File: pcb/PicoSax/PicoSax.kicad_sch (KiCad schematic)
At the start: 73 parts, among them J3 Conn_01x02, SW8va1 Omron_B3K_L13L, SW8vb1 Omron_B3K_L13L, U1 Perfboard

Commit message: Clean and Parts BOM
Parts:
- R16: footprint Resistor_THT:R_Axial_DIN0204_L3.6mm_D1.6mm_P7.62mm_Horizontal -> Resistor_SMD:R_1210_3225Metric_Pad1.30x2.65mm_HandSolder
- R17: footprint Resistor_THT:R_Axial_DIN0204_L3.6mm_D1.6mm_P7.62mm_Horizontal -> Resistor_SMD:R_0805_2012Metric_Pad1.20x1.40mm_HandSolder
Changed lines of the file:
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@@
 			)
 		)
-		(property "Footprint" "Resistor_THT:R_Axial_DIN0204_L3.6mm_D1.6mm_P7.62mm_Horizontal"
+		(property "Footprint" "Resistor_SMD:R_1210_3225Metric_Pad1.30x2.65mm_HandSolder"
 			(at 135.382 73.66 90)
 			(effects
@@
 			)
 		)
-		(property "Footprint" "Resistor_THT:R_Axial_DIN0204_L3.6mm_D1.6mm_P7.62mm_Horizontal"
+		(property "Footprint" "Resistor_SMD:R_0805_2012Metric_Pad1.20x1.40mm_HandSolder"
 			(at 135.382 83.82 90)
 			(effects

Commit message: v0.2
Updated LED footprint to have correct pin numbering.  Redid layout and traces. Added helpful silkscreen for pi pico.  Added some datasheets.
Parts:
- D10: renamed from L9; footprint MyLibrary:19-C47&slash_RSGHBHC-5V01&slash_2T_EVE-M -> PicoSax:19-C47_RSGHBHC-5V01-2T
- D11: renamed from L10; footprint MyLibrary:19-C47&slash_RSGHBHC-5V01&slash_2T_EVE-M -> PicoSax:19-C47_RSGHBHC-5V01-2T
- D12: renamed from L11; footprint MyLibrary:19-C47&slash_RSGHBHC-5V01&slash_2T_EVE-M -> PicoSax:19-C47_RSGHBHC-5V01-2T
- D13: renamed from L12; footprint MyLibrary:19-C47&slash_RSGHBHC-5V01&slash_2T_EVE-M -> PicoSax:19-C47_RSGHBHC-5V01-2T
- D14: renamed from L13; footprint MyLibrary:19-C47&slash_RSGHBHC-5V01&slash_2T_EVE-M -> PicoSax:19-C47_RSGHBHC-5V01-2T
- D2: renamed from L1; footprint MyLibrary:19-C47&slash_RSGHBHC-5V01&slash_2T_EVE-M -> PicoSax:19-C47_RSGHBHC-5V01-2T
- D3: renamed from L2; footprint MyLibrary:19-C47&slash_RSGHBHC-5V01&slash_2T_EVE-M -> PicoSax:19-C47_RSGHBHC-5V01-2T
- D4: renamed from L3; footprint MyLibrary:19-C47&slash_RSGHBHC-5V01&slash_2T_EVE-M -> PicoSax:19-C47_RSGHBHC-5V01-2T
- D5: renamed from L4; footprint MyLibrary:19-C47&slash_RSGHBHC-5V01&slash_2T_EVE-M -> PicoSax:19-C47_RSGHBHC-5V01-2T
- D6: renamed from L5; footprint MyLibrary:19-C47&slash_RSGHBHC-5V01&slash_2T_EVE-M -> PicoSax:19-C47_RSGHBHC-5V01-2T
- D7: renamed from L6; footprint MyLibrary:19-C47&slash_RSGHBHC-5V01&slash_2T_EVE-M -> PicoSax:19-C47_RSGHBHC-5V01-2T
- D8: renamed from L7; footprint MyLibrary:19-C47&slash_RSGHBHC-5V01&slash_2T_EVE-M -> PicoSax:19-C47_RSGHBHC-5V01-2T
- D9: renamed from L8; footprint MyLibrary:19-C47&slash_RSGHBHC-5V01&slash_2T_EVE-M -> PicoSax:19-C47_RSGHBHC-5V01-2T
- J2: footprint MyLibrary:MIDI_DIN5 -> PicoSax:MIDI_DIN5
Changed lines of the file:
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@@
 		(dnp no)
 		(fields_autoplaced yes)
-		(property "Reference" "L4"
+		(property "Reference" "D5"
 			(at 283.21 143.51 0)
 			(effects
@@
 			)
 		)
-		(property "Footprint" "MyLibrary:19-C47&slash_RSGHBHC-5V01&slash_2T_EVE-M"
+		(property "Footprint" "PicoSax:19-C47_RSGHBHC-5V01-2T"
 			(at 265.684 141.732 0)
 			(effects
@@
 			(project "PicoSax"
 				(path "/ef0a1a94-772b-4785-b748-662adf24a5cd"
-					(reference "L4")
+					(reference "D5")
 					(unit 1)
 				)
@@
 		(dnp no)
 		(fields_autoplaced yes)
-		(property "Reference" "L13"
+		(property "Reference" "D14"
 			(at 353.06 184.15 0)
 			(effects
@@
 			)
 		)
-		(property "Footprint" "MyLibrary:19-C47&slash_RSGHBHC-5V01&slash_2T_EVE-M"
+		(property "Footprint" "PicoSax:19-C47_RSGHBHC-5V01-2T"
 			(at 335.534 182.372 0)
 			(effects
@@
 			(project "PicoSax"
 				(path "/ef0a1a94-772b-4785-b748-662adf24a5cd"
-					(reference "L13")
+					(reference "D14")
 					(unit 1)
 				)
@@
 		(dnp no)
 		(fields_autoplaced yes)
-		(property "Reference" "L9"
+		(property "Reference" "D10"
 			(at 353.06 102.87 0)
 			(effects
@@
 			)
 		)
-		(property "Footprint" "MyLibrary:19-C47&slash_RSGHBHC-5V01&slash_2T_EVE-M"
+		(property "Footprint" "PicoSax:19-C47_RSGHBHC-5V01-2T"
 			(at 335.534 101.092 0)
 			(effects
@@
 			(project "PicoSax"
 				(path "/ef0a1a94-772b-4785-b748-662adf24a5cd"
-					(reference "L9")
+					(reference "D10")
 					(unit 1)
 				)
@@
 			)
 		)
-		(property "Footprint" "MyLibrary:MIDI_DIN5"
+		(property "Footprint" "PicoSax:MIDI_DIN5"
 			(at 152.4 67.31 0)
 			(effects
@@
 		(dnp no)
 		(fields_autoplaced yes)
-		(property "Reference" "L6"
+		(property "Reference" "D7"
 			(at 283.21 184.15 0)
 			(effects
@@
 			)
 		)
-		(property "Footprint" "MyLibrary:19-C47&slash_RSGHBHC-5V01&slash_2T_EVE-M"
+		(property "Footprint" "PicoSax:19-C47_RSGHBHC-5V01-2T"
 			(at 265.684 182.372 0)
 			(effects
@@
 			(project ""
 				(path "/ef0a1a94-772b-4785-b748-662adf24a5cd"
-					(reference "L6")
+					(reference "D7")
 					(unit 1)
 				)
@@
 		(dnp no)
 		(fields_autoplaced yes)
-		(property "Reference" "L5"
+		(property "Reference" "D6"
 			(at 283.21 163.83 0)
 			(effects
@@
 			)
 		)
-		(property "Footprint" "MyLibrary:19-C47&slash_RSGHBHC-5V01&slash_2T_EVE-M"
+		(property "Footprint" "PicoSax:19-C47_RSGHBHC-5V01-2T"
 			(at 265.684 162.052 0)
 			(effects
@@
 			(project "PicoSax"
 				(path "/ef0a1a94-772b-4785-b748-662adf24a5cd"
-					(reference "L5")
+					(reference "D6")
 					(unit 1)
 				)
@@
 		(dnp no)
 		(fields_autoplaced yes)
-		(property "Reference" "L10"
+		(property "Reference" "D11"
 			(at 353.06 123.19 0)
 			(effects
@@
 			)
 		)
-		(property "Footprint" "MyLibrary:19-C47&slash_RSGHBHC-5V01&slash_2T_EVE-M"
+		(property "Footprint" "PicoSax:19-C47_RSGHBHC-5V01-2T"
 			(at 335.534 121.412 0)
 			(effects
@@
 			(project "PicoSax"
 				(path "/ef0a1a94-772b-4785-b748-662adf24a5cd"
-					(reference "L10")
+					(reference "D11")
 					(unit 1)
 				)
@@
 	)
 	(symbol
-		(lib_name "MP3V5004GP_1")
 		(lib_id "PicoSax:MP3V5004GP_1")
 		(at 212.09 187.96 0)
@@
 		(dnp no)
 		(fields_autoplaced yes)
-		(property "Reference" "L8"
+		(property "Reference" "D9"
 			(at 353.06 82.55 0)
 			(effects
@@
 			)
 		)
-		(property "Footprint" "MyLibrary:19-C47&slash_RSGHBHC-5V01&slash_2T_EVE-M"
+		(property "Footprint" "PicoSax:19-C47_RSGHBHC-5V01-2T"
 			(at 335.534 80.772 0)
 			(effects
@@
 			(project "PicoSax"
 				(path "/ef0a1a94-772b-4785-b748-662adf24a5cd"
-					(reference "L8")
+					(reference "D9")
 					(unit 1)
 				)
@@
 		(dnp no)
 		(fields_autoplaced yes)
-		(property "Reference" "L2"
+		(property "Reference" "D3"
 			(at 283.21 102.87 0)
 			(effects
@@
 			)
 		)
-		(property "Footprint" "MyLibrary:19-C47&slash_RSGHBHC-5V01&slash_2T_EVE-M"
+		(property "Footprint" "PicoSax:19-C47_RSGHBHC-5V01-2T"
 			(at 265.684 101.092 0)
 			(effects
@@
 			(project "PicoSax"
 				(path "/ef0a1a94-772b-4785-b748-662adf24a5cd"
-					(reference "L2")
+					(reference "D3")
 					(unit 1)
 				)
@@
 		(dnp no)
 		(fields_autoplaced yes)
-		(property "Reference" "L1"
+		(property "Reference" "D2"
 			(at 283.21 82.55 0)
 			(effects
@@
 			)
 		)
-		(property "Footprint" "MyLibrary:19-C47&slash_RSGHBHC-5V01&slash_2T_EVE-M"
+		(property "Footprint" "PicoSax:19-C47_RSGHBHC-5V01-2T"
 			(at 265.684 80.772 0)
 			(effects
@@
 			(project "PicoSax"
 				(path "/ef0a1a94-772b-4785-b748-662adf24a5cd"
-					(reference "L1")
+					(reference "D2")
 					(unit 1)
 				)
@@
 		(dnp no)
 		(fields_autoplaced yes)
-		(property "Reference" "L3"
+		(property "Reference" "D4"
 			(at 283.21 123.19 0)
 			(effects
@@
 			)
 		)
-		(property "Footprint" "MyLibrary:19-C47&slash_RSGHBHC-5V01&slash_2T_EVE-M"
+		(property "Footprint" "PicoSax:19-C47_RSGHBHC-5V01-2T"
 			(at 265.684 121.412 0)
 			(effects
@@
 			(project "PicoSax"
 				(path "/ef0a1a94-772b-4785-b748-662adf24a5cd"
-					(reference "L3")
+					(reference "D4")
 					(unit 1)
 				)
@@
 		(dnp no)
 		(fields_autoplaced yes)
-		(property "Reference" "L7"
+		(property "Reference" "D8"
 			(at 353.06 60.96 0)
 			(effects
@@
 			)
 		)
-		(property "Footprint" "MyLibrary:19-C47&slash_RSGHBHC-5V01&slash_2T_EVE-M"
+		(property "Footprint" "PicoSax:19-C47_RSGHBHC-5V01-2T"
 			(at 335.534 59.182 0)
 			(effects
@@
 			(project "PicoSax"
 				(path "/ef0a1a94-772b-4785-b748-662adf24a5cd"
-					(reference "L7")
+					(reference "D8")
 					(unit 1)
 				)
@@
 		(dnp no)
 		(fields_autoplaced yes)
-		(property "Reference" "L11"
+		(property "Reference" "D12"
 			(at 353.06 143.51 0)
 			(effects
@@
 			)
 		)
-		(property "Footprint" "MyLibrary:19-C47&slash_RSGHBHC-5V01&slash_2T_EVE-M"
+		(property "Footprint" "PicoSax:19-C47_RSGHBHC-5V01-2T"
 			(at 335.534 141.732 0)
 			(effects
@@
 			(project "PicoSax"
 				(path "/ef0a1a94-772b-4785-b748-662adf24a5cd"
-					(reference "L11")
+					(reference "D12")
 					(unit 1)
 				)
@@
 		(dnp no)
 		(fields_autoplaced yes)
-		(property "Reference" "L12"
+		(property "Reference" "D13"
 			(at 353.06 163.83 0)
 			(effects
@@
 			)
 		)
-		(property "Footprint" "MyLibrary:19-C47&slash_RSGHBHC-5V01&slash_2T_EVE-M"
+		(property "Footprint" "PicoSax:19-C47_RSGHBHC-5V01-2T"
 			(at 335.534 162.052 0)
 			(effects
@@
 			(project "PicoSax"
 				(path "/ef0a1a94-772b-4785-b748-662adf24a5cd"
-					(reference "L12")
+					(reference "D13")
 					(unit 1)
 				)

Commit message: move air pressure
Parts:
- U1: footprint MyLibrary:Perfboard 12x20 -> MyLibrary:Perfboard 10x20; now left out of the parts list
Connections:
- net +3V3: now also U1.1 (Top_Rail)
- net GND: now also U1.2 (Bottom_Rail)
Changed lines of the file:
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@@
 	(symbol
 		(lib_id "PicoSax:GND")
+		(at 201.93 59.69 0)
+		(unit 1)
+		(exclude_from_sim no)
+		(in_bom yes)
+		(on_board yes)
+		(dnp no)
+		(fields_autoplaced yes)
+		(property "Reference" "#PWR091"
+			(at 201.93 66.04 0)
+			(effects
+				(font
+					(size 1.27 1.27)
+				)
+				(hide yes)
+			)
+		)
+		(property "Value" "GND"
+			(at 201.93 64.77 0)
+			(effects
+				(font
+					(size 1.27 1.27)
+				)
+			)
+		)
+		(property "Footprint" ""
+			(at 201.93 59.69 0)
+			(effects
+				(font
+					(size 1.27 1.27)
+				)
+				(hide yes)
+			)
+		)
+		(property "Datasheet" ""
+			(at 201.93 59.69 0)
+			(effects
+				(font
+					(size 1.27 1.27)
+				)
+				(hide yes)
+			)
+		)
+		(property "Description" "Power symbol creates a global label with name \"GND\" , ground"
+			(at 201.93 59.69 0)
+			(effects
+				(font
+					(size 1.27 1.27)
+				)
+				(hide yes)
+			)
+		)
+		(pin "1"
+		)
+		(instances
+			(project ""
+				(path "/ef0a1a94-772b-4785-b748-662adf24a5cd"
+					(reference "#PWR091")
+					(unit 1)
+				)
+			)
+		)
+	)
+	(symbol
+		(lib_id "PicoSax:GND")
 		(at 373.38 92.71 90)
 		(unit 1)
@@
 	)
 	(symbol
+		(lib_id "PicoSax:+3V3")
+		(at 181.61 53.34 0)
+		(unit 1)
+		(exclude_from_sim no)
+		(in_bom yes)
+		(on_board yes)
+		(dnp no)
+		(fields_autoplaced yes)
+		(property "Reference" "#PWR090"
+			(at 181.61 57.15 0)
+			(effects
+				(font
+					(size 1.27 1.27)
+				)
+				(hide yes)
+			)
+		)
+		(property "Value" "+3V3"
+			(at 181.61 48.26 0)
+			(effects
+				(font
+					(size 1.27 1.27)
+				)
+			)
+		)
+		(property "Footprint" ""
+			(at 181.61 53.34 0)
+			(effects
+				(font
+					(size 1.27 1.27)
+				)
+				(hide yes)
+			)
+		)
+		(property "Datasheet" ""
+			(at 181.61 53.34 0)
+			(effects
+				(font
+					(size 1.27 1.27)
+				)
+				(hide yes)
+			)
+		)
+		(property "Description" "Power symbol creates a global label with name \"+3V3\""
+			(at 181.61 53.34 0)
+			(effects
+				(font
+					(size 1.27 1.27)
+				)
+				(hide yes)
+			)
+		)
+		(pin "1"
+		)
+		(instances
+			(project ""
+				(path "/ef0a1a94-772b-4785-b748-662adf24a5cd"
+					(reference "#PWR090")
+					(unit 1)
+				)
+			)
+		)
+	)
+	(symbol
 		(lib_id "PicoSax:GND")
 		(at 227.33 140.97 270)
@@
 	(symbol
 		(lib_id "PicoSax:Perfboard")
-		(at 180.34 62.23 0)
+		(at 186.69 55.88 0)
 		(unit 1)
 		(exclude_from_sim no)
-		(in_bom yes)
+		(in_bom no)
 		(on_board yes)
 		(dnp no)
 		(fields_autoplaced yes)
 		(property "Reference" "U1"
-			(at 186.69 63.4999 0)
+			(at 193.04 57.1499 0)
 			(effects
 				(font
@@
 		)
 		(property "Value" "Perfboard"
-			(at 186.69 65.405 0)
+			(at 193.04 59.055 0)
 			(effects
 				(font
 					(size 1.27 1.27)
 				)
-				(justify left)
+				(justify bottom)
 			)
 		)
-		(property "Footprint" "MyLibrary:Perfboard 12x20"
-			(at 180.34 62.23 0)
+		(property "Footprint" "MyLibrary:Perfboard 10x20"
+			(at 186.69 55.88 0)
 			(effects
 				(font
 					(size 1.27 1.27)
 				)
-				(hide yes)
 			)
 		)
 		(property "Datasheet" ""
-			(at 180.34 62.23 0)
+			(at 186.69 55.88 0)
 			(effects
 				(font
@@
 		)
 		(property "Description" ""
-			(at 180.34 62.23 0)
+			(at 186.69 55.88 0)
 			(effects
 				(font
@@
 			)
 		)
+		(pin "2"
+		)
+		(pin "1"
+		)
 		(instances

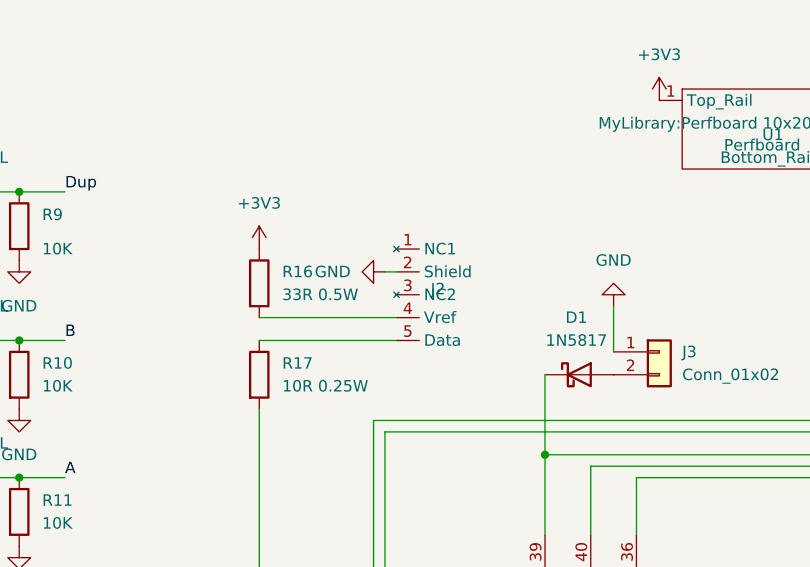
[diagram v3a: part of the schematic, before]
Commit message: Mouthpiece mounting hole update
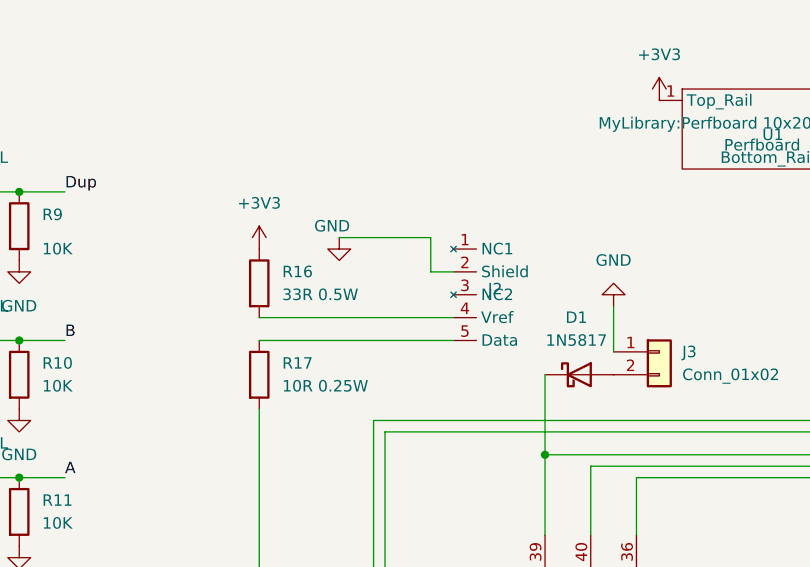
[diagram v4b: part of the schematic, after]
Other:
- moved on the sheet: J2
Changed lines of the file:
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@@
 	(wire
 		(pts
+			(xy 156.21 68.58) (xy 156.21 72.39)
+		)
+		(stroke
+			(width 0)
+			(type default)
+		)
+	)
+	(wire
+		(pts
 			(xy 373.38 124.46) (xy 373.38 115.57)
 		)
@@
 	(wire
 		(pts
-			(xy 137.16 80.01) (xy 152.4 80.01)
-		)
-		(stroke
-			(width 0)
-			(type default)
-		)
-	)
-	(wire
-		(pts
 			(xy 168.91 92.71) (xy 236.22 92.71)
 		)
@@
 	(wire
 		(pts
-			(xy 152.4 72.39) (xy 151.13 72.39)
-		)
-		(stroke
-			(width 0)
-			(type default)
-		)
-	)
-	(wire
-		(pts
 			(xy 129.54 121.92) (xy 137.16 121.92)
 		)
@@
 	(wire
 		(pts
+			(xy 156.21 72.39) (xy 158.75 72.39)
+		)
+		(stroke
+			(width 0)
+			(type default)
+		)
+	)
+	(wire
+		(pts
 			(xy 106.68 95.25) (xy 110.49 95.25)
 		)
@@
 	(wire
 		(pts
+			(xy 137.16 77.47) (xy 158.75 77.47)
+		)
+		(stroke
+			(width 0)
+			(type default)
+		)
+	)
+	(wire
+		(pts
 			(xy 129.54 167.64) (xy 137.16 167.64)
 		)
@@
 	(wire
 		(pts
-			(xy 137.16 77.47) (xy 152.4 77.47)
-		)
-		(stroke
-			(width 0)
-			(type default)
-		)
-	)
-	(wire
-		(pts
 			(xy 262.89 104.14) (xy 303.53 104.14)
 		)
@@
 	(wire
 		(pts
+			(xy 146.05 68.58) (xy 156.21 68.58)
+		)
+		(stroke
+			(width 0)
+			(type default)
+		)
+	)
+	(wire
+		(pts
 			(xy 212.09 176.53) (xy 201.93 176.53)
 		)
@@
 	(wire
 		(pts
+			(xy 137.16 80.01) (xy 158.75 80.01)
+		)
+		(stroke
+			(width 0)
+			(type default)
+		)
+	)
+	(wire
+		(pts
 			(xy 151.13 129.54) (xy 146.05 129.54)
 		)
@@
 	(symbol
 		(lib_id "PicoSax:MIDI_DIN5")
-		(at 152.4 67.31 0)
+		(at 158.75 67.31 0)
 		(unit 1)
 		(exclude_from_sim no)
@@
 		(fields_autoplaced yes)
 		(property "Reference" "J2"
-			(at 156.21 74.2949 0)
+			(at 162.56 74.2949 0)
 			(effects
 				(font
@@
 		)
 		(property "Value" "~"
-			(at 156.21 76.2 0)
+			(at 162.56 76.2 0)
 			(effects
 				(font
@@
 		)
 		(property "Footprint" "PicoSax:MIDI_DIN5"
-			(at 152.4 67.31 0)
+			(at 158.75 67.31 0)
 			(effects
 				(font
@@
 		)
 		(property "Datasheet" ""
-			(at 152.4 67.31 0)
+			(at 158.75 67.31 0)
 			(effects
 				(font
@@
 		)
 		(property "Description" ""
-			(at 152.4 67.31 0)
+			(at 158.75 67.31 0)
 			(effects
 				(font
@@
 	(symbol
 		(lib_id "PicoSax:GND")
-		(at 151.13 72.39 270)
+		(at 146.05 68.58 0)
 		(unit 1)
 		(exclude_from_sim no)
@@
 		(on_board yes)
 		(dnp no)
-		(fields_autoplaced yes)
 		(property "Reference" "#PWR036"
-			(at 144.78 72.39 0)
+			(at 146.05 74.93 0)
 			(effects
 				(font
@@
 		)
 		(property "Value" "GND"
-			(at 147.32 72.3899 90)
+			(at 143.256 67.31 0)
 			(effects
 				(font
 					(size 1.27 1.27)
 				)
-				(justify right)
+				(justify left)
 			)
 		)
 		(property "Footprint" ""
-			(at 151.13 72.39 0)
+			(at 146.05 68.58 0)
 			(effects
 				(font
@@
 		)
 		(property "Datasheet" ""
-			(at 151.13 72.39 0)
+			(at 146.05 68.58 0)
 			(effects
 				(font
@@
 		)
 		(property "Description" "Power symbol creates a global label with name \"GND\" , ground"
-			(at 151.13 72.39 0)
+			(at 146.05 68.58 0)
 			(effects
 				(font
